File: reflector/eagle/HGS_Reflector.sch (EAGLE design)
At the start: 25 parts, among them J1 U.FL, U3 LP2985XX-N

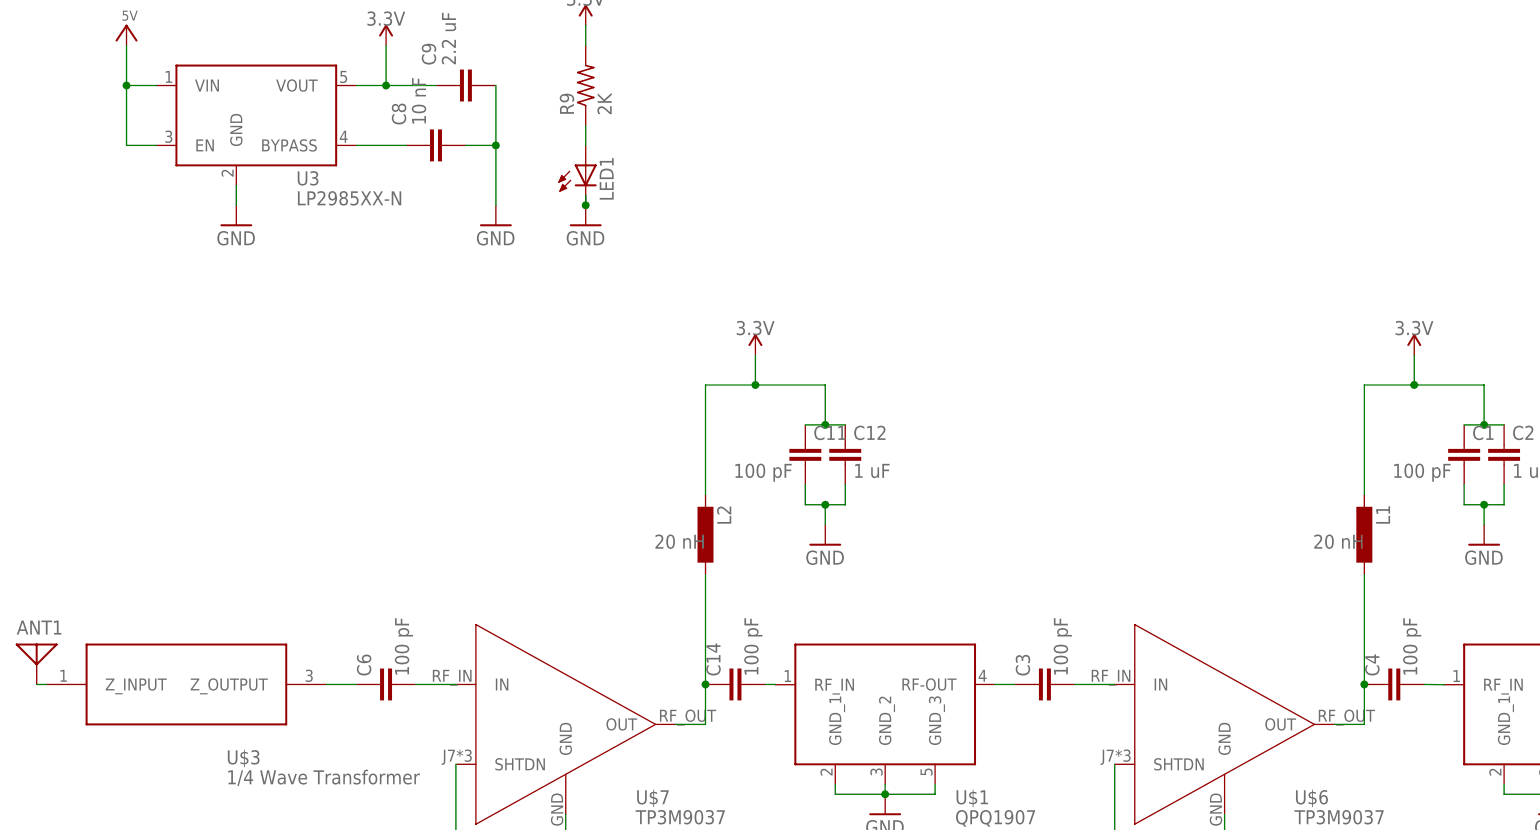
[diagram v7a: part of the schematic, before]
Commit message: I've completed the BOM for version 1 of the PCB for the reflector. Regarding the board and schematic themselves, the board needs to be mapped out with all parts oriented before being reviewed.
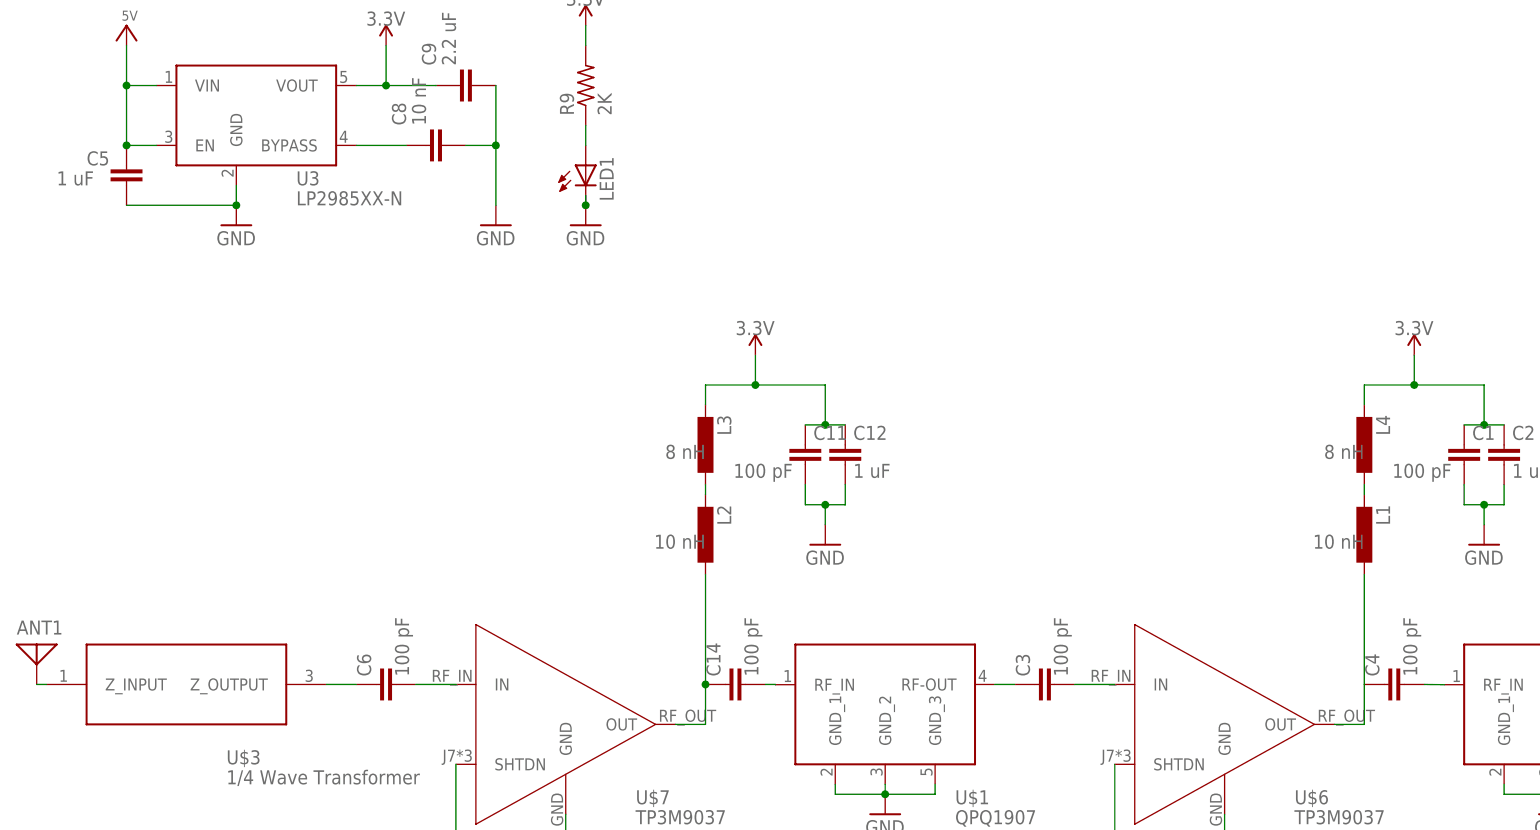
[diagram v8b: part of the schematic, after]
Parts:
- added C5: 1 uF, ngspice-simulation:C
- added L3, L4: (no value), rcl:L-EUL3216C
- L1, L2: SPICEPREFIX 20 nH -> 10 nH
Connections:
- new net 3.3V1: L4.2
- new net N$13: L1.1
- new net N$14: L1.2, L4.1
- new net N$7: L2.2, L3.1
- net 3.3V: now also L3.2; no longer L1.2, L2.2
- net 5V: now also C5.1
- net GND: now also C5.2
- net N$2: no longer L1.1
